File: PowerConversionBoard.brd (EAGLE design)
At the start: 72.4 x 71.1 mm, 33 parts, among them U3 AZ1117EH-3.3TRG1

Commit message: routed the board
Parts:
- removed C24: 150uF, PowerComponents:CTAN(7.30_4.30MM)
- removed U$2: DIST_TO_CONV, Dist_To_Conv_Connector:DIST_TO_CONV
- removed U$4: SWITCHMODE_SCHOTTKY, PowerComponents:DPAK-3
- removed U$7: HCM1305, HCM1305:HCM1305
- added COUT: 100uF, PowerComponents:CTAN(7.30_4.30MM)
- added D1: SWITCHMODE_SCHOTTKY, PowerComponents:DPAK-3
- added L1: HCM1305, HCM1305:HCM1305
- added U$3: CON2DIST, Dist_Convert_Connector:CON2DIST
- CIN: value 47uF -> 3.33uF
- moved RSEN 96.0 mm to (48.5, 43.7), turned to 90 degrees
- moved D2 67.3 mm to (2.03, 12.2)
- moved D3 67.3 mm to (2.03, 8.13)
- moved D4 67.3 mm to (2.03, 4.32)
- moved 5R 55.2 mm to (5.59, 13.2)
- moved 3R 53.2 mm to (5.84, 9.40)
- moved 1R 52.9 mm to (5.59, 4.32)
- moved U3 51.3 mm to (51.6, 13.2)
- moved +3.3 47.0 mm to (66.9, 4.33)
- moved Q1 33.7 mm to (45.8, 35.4), turned to 180 degrees
- moved 5V_3.3_TP 31.6 mm to (66.6, 12.6)
- moved CIN 29.0 mm to (34.8, 38.6), turned to 270 degrees
- moved COUPLE 28.8 mm to (31.0, 12.2), turned to 90 degrees
- moved +3.3V 25.8 mm to (67.4, 53.2)
- moved 5V_3.3 23.1 mm to (53.9, 52.5)
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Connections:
- net +3.3V: now also U$3.4; no longer U$2.3V, U$2.48V
- net +48V: now also U$3.1@1, U$3.1@2
- net +5V: now also COUT.+, L1.2, U$3.3@1, U$3.3@2, U$3.3@3; no longer C24.+, U$2.5V_1, U$2.5V_2, U$2.5V_3, U$2.5V_4, U$7.2
- net GND: now also COUT.-, D1.P$1, D1.P$3, U$3.2@1, U$3.2@2, U$3.5@1, U$3.5@2, U$3.5@3, U$3.5@4; no longer C24.-, U$2.GND_1, U$2.GND_2, U$2.GND_3, U$2.GND_4, U$4.P$1, U$4.P$3
- net N$10: now also D1.P$4, L1.1; no longer U$4.P$4, U$7.1
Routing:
- net GND: track 0.00 -> 276.6 mm
- net +5V: track 0.00 -> 252.0 mm, vias 0 -> 3
- net +3.3V: track 0.00 -> 211.6 mm
- net +48V: track 0.00 -> 121.8 mm
- net N$13: track 0.00 -> 65.2 mm
- net N$10: track 0.00 -> 48.7 mm, vias 0 -> 2
- net N$11: track 0.00 -> 35.8 mm
- net N$7: track 0.00 -> 26.7 mm
- net N$9: track 0.00 -> 23.5 mm, vias 0 -> 2
- net N$12: track 0.00 -> 19.8 mm
- net N$1: track 0.00 -> 9.93 mm
- net N$3: track 0.00 -> 5.20 mm
- net N$5: track 0.00 -> 5.15 mm
- net N$4: track 0.00 -> 4.94 mm
- net N$6: track 0.00 -> 4.57 mm

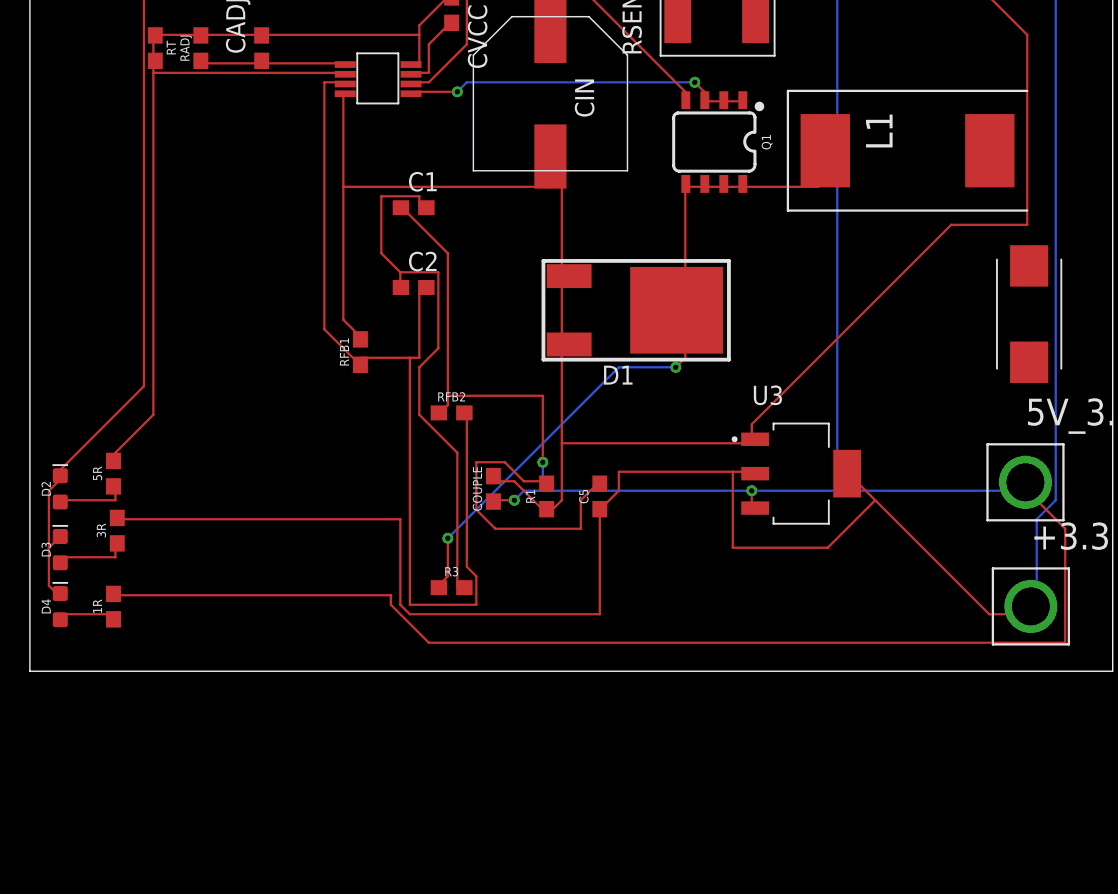
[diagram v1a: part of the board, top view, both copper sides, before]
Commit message: wrong inductor previously. oops
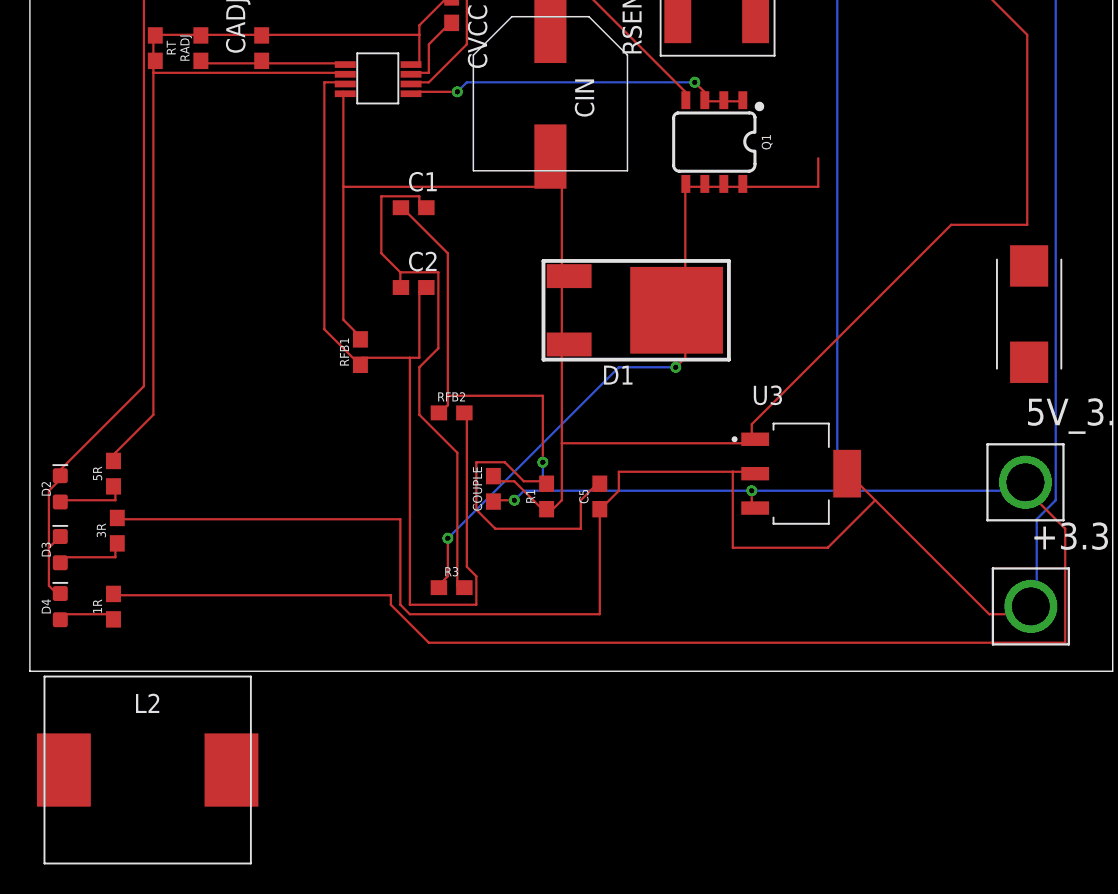
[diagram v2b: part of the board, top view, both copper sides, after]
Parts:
- removed L1: HCM1305, HCM1305:HCM1305
- added L2: 15uH, Inductor_15uH - hcma1305:HCMA1305
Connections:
- net +5V: now also L2.2; no longer L1.2
- net N$10: now also L2.1; no longer L1.1
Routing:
- net N$10: track 48.7 -> 48.0 mm
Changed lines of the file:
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@@
 <?xml version="1.0" encoding="utf-8"?>
 <!DOCTYPE eagle SYSTEM "eagle.dtd">
-<eagle version="9.6.2">
+<eagle version="9.5.0">
 <drawing>
 <settings>
@@
 <vertex x="40.132" y="33.274"/>
 <vertex x="29.464" y="33.274"/>
-</polygon>
-<polygon width="0.1524" layer="41">
-<vertex x="53.34" y="38.862"/>
-<vertex x="53.34" y="30.734"/>
-<vertex x="64.516" y="30.734"/>
-<vertex x="64.516" y="38.862"/>
 </polygon>
 <polygon width="0.1524" layer="41">
@@
 </element>
 <element name="COUT" library="PowerComponents" package="CTAN(7.30_4.30MM)" value="100uF" x="66.802" y="23.876" smashed="yes" rot="R270"/>
-<element name="L1" library="HCM1305" package="HCM1305" value="HCM1305" x="58.674" y="34.798" smashed="yes" rot="R90">
-<attribute name="NAME" x="57.674" y="34.798" size="1.778" layer="25" rot="R90"/>
-</element>
 <element name="D1" library="PowerComponents" package="DPAK-3" value="SWITCHMODE_SCHOTTKY" x="40.132" y="24.13" smashed="yes" rot="R180">
 <attribute name="NAME" x="40.432" y="20.43" size="1.27" layer="25" rot="R180"/>
@@
 </element>
 <element name="U$3" library="Dist_Convert_Connector" package="CON2DIST" value="CON2DIST" x="36.576" y="64.516" smashed="yes" rot="R270"/>
+<element name="L2" library="Inductor_15uH - hcma1305" package="HCMA1305" package3d_urn="urn:adsk.eagle:package:24201702/2" value="15uH" x="7.874" y="-6.604" smashed="yes">
+<attribute name="NAME" x="7.874" y="-2.794" size="1.27" layer="25" align="bottom-center"/>
+<attribute name="VALUE" x="7.874" y="-10.414" size="1.27" layer="27" align="top-center"/>
+</element>
 </elements>
 <signals>
@@
 <contactref element="C1" pad="1"/>
 <contactref element="RFB2" pad="1"/>
-<contactref element="L1" pad="2"/>
 <contactref element="COUT" pad="+"/>
 <contactref element="U$3" pad="3@3"/>
@@
 <via x="48.26" y="12.065" extent="1-16" drill="0.35"/>
 <via x="34.29" y="13.97" extent="1-16" drill="0.35"/>
-<wire x1="66.802" y1="27.096" x2="64.174" y2="34.798" width="0" layer="19" extent="1-1"/>
+<contactref element="L2" pad="2"/>
 <wire x1="66.556984375" y1="12.62994375" x2="66.802" y2="27.096" width="0" layer="19" extent="1-1"/>
+<wire x1="13.474" y1="-6.604" x2="5.588" y2="5.168" width="0" layer="19" extent="1-1"/>
 </signal>
 <signal name="N$4">
@@
 <contactref element="Q1" pad="8"/>
 <contactref element="R3" pad="1"/>
-<contactref element="L1" pad="1"/>
 <contactref element="D1" pad="P$4"/>
 <wire x1="45.085" y1="32.385" x2="43.815" y2="32.385" width="0.1524" layer="1"/>
@@
 <wire x1="52.705" y1="34.29" x2="52.705" y2="32.385" width="0.1524" layer="1"/>
 <wire x1="47.625" y1="32.385" x2="47.660665625" y2="32.57548125" width="0.1524" layer="1"/>
-<wire x1="52.705" y1="34.29" x2="53.174" y2="34.798" width="0.1524" layer="1"/>
 <wire x1="27.94" y1="6.35" x2="27.305" y2="5.715" width="0.1524" layer="1"/>
 <wire x1="27.94" y1="8.89" x2="27.94" y2="6.35" width="0.1524" layer="1"/>
@@
 <via x="27.94" y="8.89" extent="1-16" drill="0.35"/>
 <via x="43.18" y="20.32" extent="1-16" drill="0.35"/>
+<contactref element="L2" pad="1"/>
+<wire x1="2.274" y1="-6.604" x2="27.344" y2="5.588" width="0" layer="19" extent="1-1"/>
 </signal>
 <signal name="N$11">

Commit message: routed everything (except ground) hopefully right
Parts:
- moved L2 69.8 mm to (61.2, 38.4), turned to 180 degrees
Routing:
- net +5V: track 252.0 -> 282.7 mm, vias 3 -> 2
- net N$13: track 65.2 -> 34.8 mm, vias 0 -> 2
- net N$10: track 48.0 -> 74.9 mm, vias 2 -> 0
- net N$12: track 19.8 -> 3.89 mm
- net N$11: track 35.8 -> 49.5 mm
- net N$9: track 23.5 -> 36.7 mm, vias 2 -> 0
- net +3.3V: track 211.6 -> 221.8 mm, vias 0 -> 2
- net +48V: track 121.8 -> 131.9 mm, vias 0 -> 4
- net N$7: track 26.7 -> 18.9 mm, vias 0 -> 2
- net GND: track 276.6 -> 282.2 mm
- net N$6: track 4.57 -> 3.76 mm
- net N$4: track 4.94 -> 4.15 mm
- net N$5: track 5.15 -> 4.51 mm

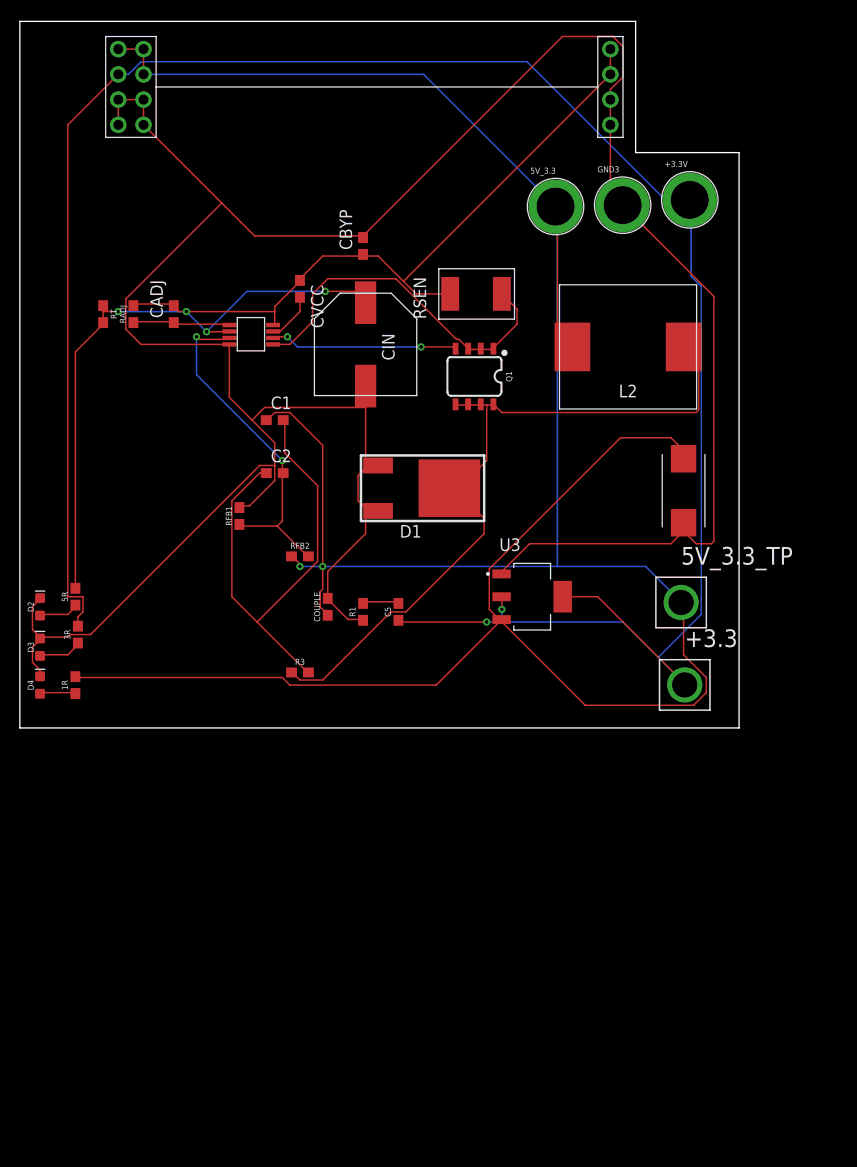
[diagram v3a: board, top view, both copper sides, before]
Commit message: Finished all the routing
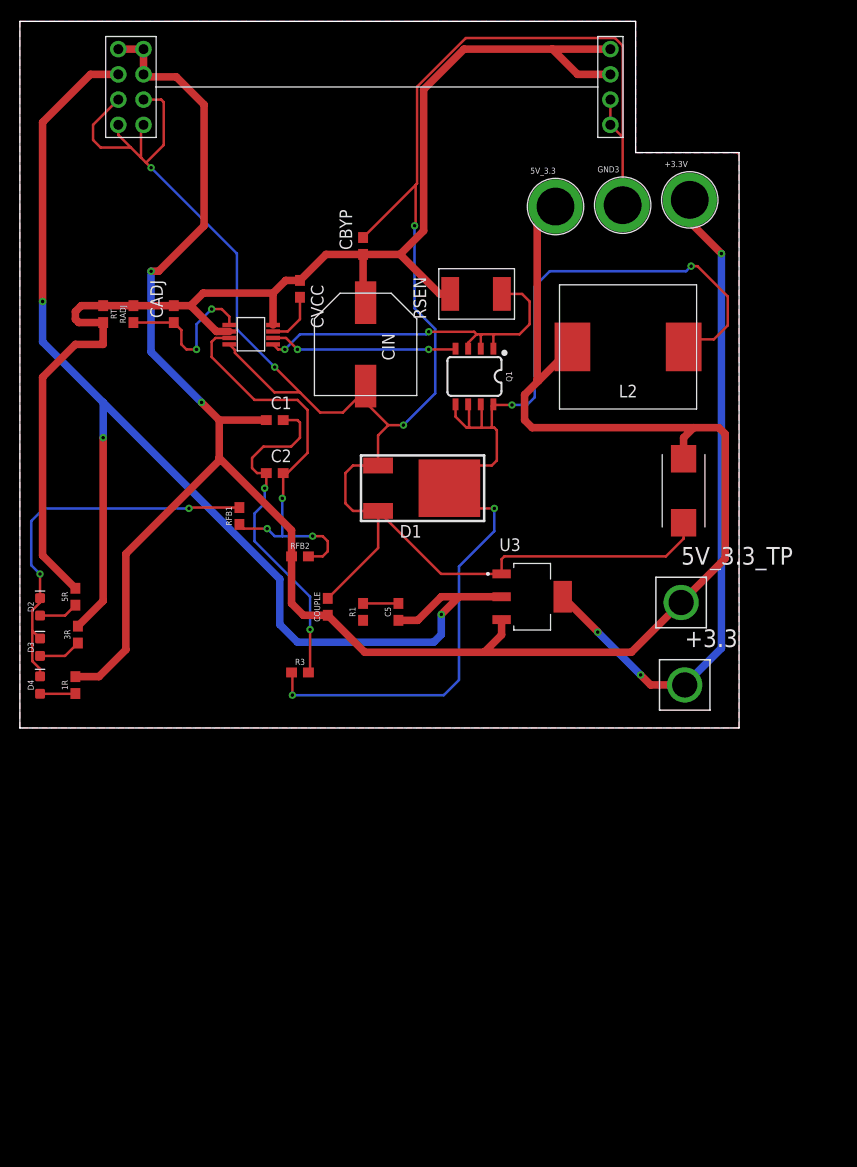
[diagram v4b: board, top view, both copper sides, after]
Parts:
- RADJ: value 9.5k -> 1.8k
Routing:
- net +5V: track 282.7 -> 223.5 mm
- net N$10: track 74.9 -> 111.4 mm, vias 0 -> 4
- net +3.3V: track 221.8 -> 194.5 mm, vias 2 -> 6
- net N$11: track 49.5 -> 34.6 mm, vias 0 -> 2
- net GND: track 282.2 -> 269.6 mm, vias 0 -> 6
- net N$13: track 34.8 -> 42.1 mm, vias 2 -> 3
- net N$1: track 10.1 -> 15.9 mm, vias 0 -> 2
- net +48V: track 131.9 -> 135.8 mm, vias 4 -> 0
- net N$9: track 36.7 -> 37.5 mm, vias 0 -> 2
- added copper zone on layer 1, net GND
- added copper zone on layer 16, net GND

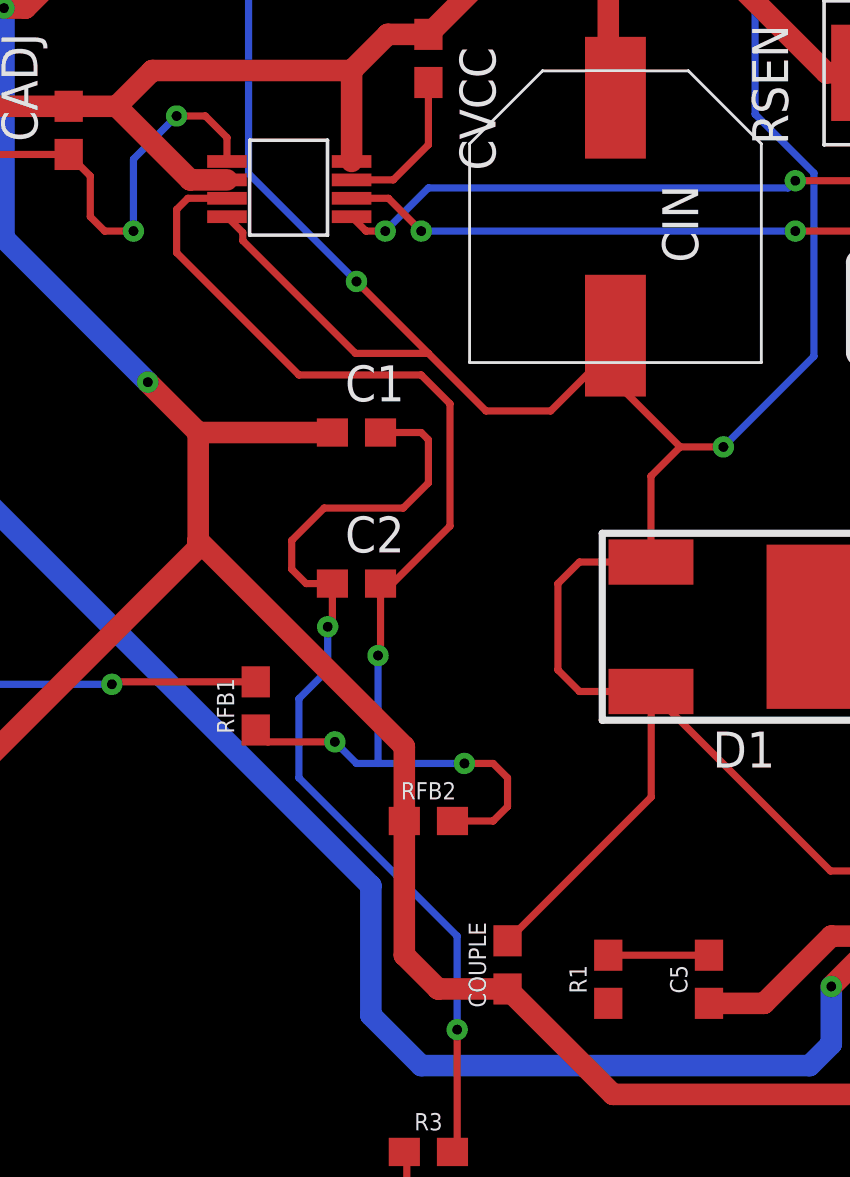
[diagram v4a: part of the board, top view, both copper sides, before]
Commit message: Fixed an air wire I missed earlier
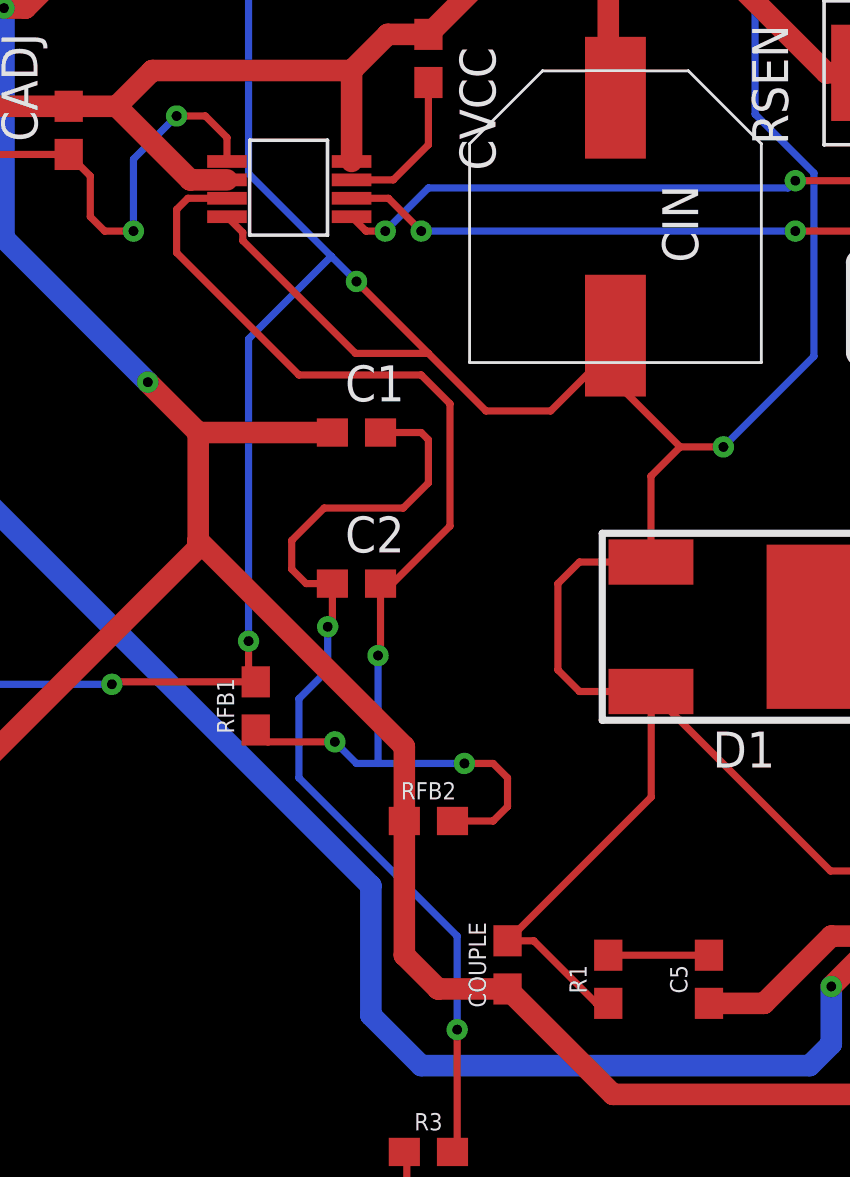
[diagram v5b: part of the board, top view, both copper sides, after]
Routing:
- net GND: track 269.6 -> 290.4 mm, vias 6 -> 7
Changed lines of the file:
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@@
 <wire x1="28.194" y1="33.782" x2="25.654" y2="36.322" width="0.254" layer="1"/>
 <via x="25.654" y="36.322" extent="1-16" drill="0.35"/>
-<wire x1="25.654" y1="36.322" x2="21.844" y2="40.132" width="0.254" layer="16"/>
+<wire x1="25.654" y1="36.322" x2="24.765" y2="37.211" width="0.254" layer="16"/>
+<wire x1="24.765" y1="37.211" x2="21.844" y2="40.132" width="0.254" layer="16"/>
 <wire x1="21.844" y1="47.752" x2="13.208" y2="56.388" width="0.254" layer="16"/>
 <via x="13.208" y="56.388" extent="1-16" drill="0.35"/>
@@
 <wire x1="60.672084375" y1="68.670446875" x2="60.672084375" y2="59.469915625" width="0.254" layer="1"/>
 <wire x1="59.89893125" y1="69.4436" x2="60.672084375" y2="68.670446875" width="0.254" layer="1"/>
-<wire x1="30.988" y1="13.042" x2="34.544" y2="10.834" width="0" layer="19" extent="1-1"/>
-<wire x1="22.098" y1="22.186" x2="30.988" y2="13.042" width="0" layer="19" extent="1-1"/>
+<wire x1="30.988" y1="13.042" x2="31.916" y2="13.042" width="0.254" layer="1"/>
+<wire x1="34.124" y1="10.834" x2="34.544" y2="10.834" width="0.254" layer="1"/>
+<wire x1="31.916" y1="13.042" x2="34.124" y2="10.834" width="0.254" layer="1"/>
+<wire x1="22.098" y1="22.186" x2="21.844" y2="22.44" width="0.254" layer="1"/>
+<wire x1="21.844" y1="22.44" x2="21.844" y2="23.622" width="0.254" layer="1"/>
+<via x="21.844" y="23.622" extent="1-16" drill="0.35"/>
+<wire x1="21.844" y1="23.622" x2="21.844" y2="34.29" width="0.254" layer="16"/>
+<wire x1="21.844" y1="34.29" x2="24.765" y2="37.211" width="0.254" layer="16"/>
 </signal>
 <signal name="+3.3V">
